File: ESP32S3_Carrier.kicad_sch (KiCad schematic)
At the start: 63 parts, among them J1 CC1101 433MHz SMA, J2 NRF24L01+PA+LNA #1, J3 NRF24L01+PA+LNA #2, J4 PN532 V3 (I2C), J5 OLED 1.3in SH1106 I2C, J6 Catalex microSD, J7 RDM6300 125kHz, J8 125kHz coil, J9 Si5351 clock gen (3x SMA), Q1 PN2222A, Q2 PN2222A, Q3 AO3401A, SW1 UP, SW2 DOWN, SW3 LEFT, SW4 RIGHT, SW5 OK, SW6 BACK, SW7 MODULE PWR, U1 ESP32-S3-DevKitC-1 N16R8, U2 AMS1117-3.3, U3 VS1838B

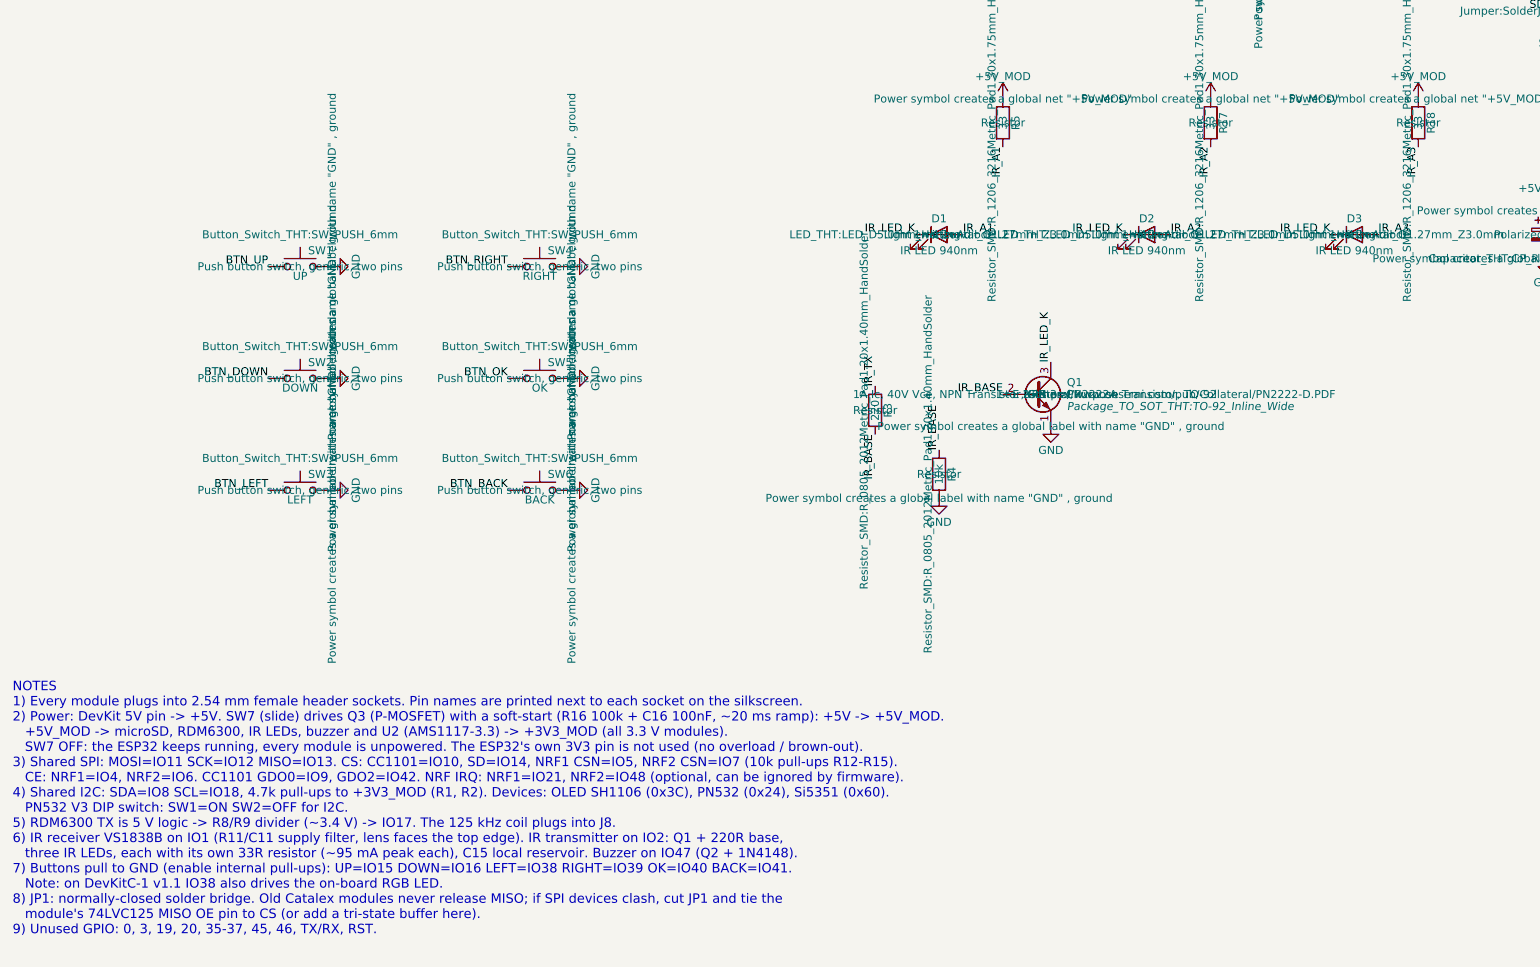
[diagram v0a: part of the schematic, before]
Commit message: IR LED resistors 33R -> 47R, README notes
- 47R per IR LED (~67 mA, ~0.21 W) so a stuck-high IO2 stays inside the 1206 rating
- README: drive IO2 only with the 38 kHz carrier; how to handle starved_thermal after a re-route

Co-Authored-By: Claude Opus 5.5 <noreply@anthropic.com>
Claude-Session: https://claude.ai/code/session_01M7B8FMVeVb1bqPRBZwSV29
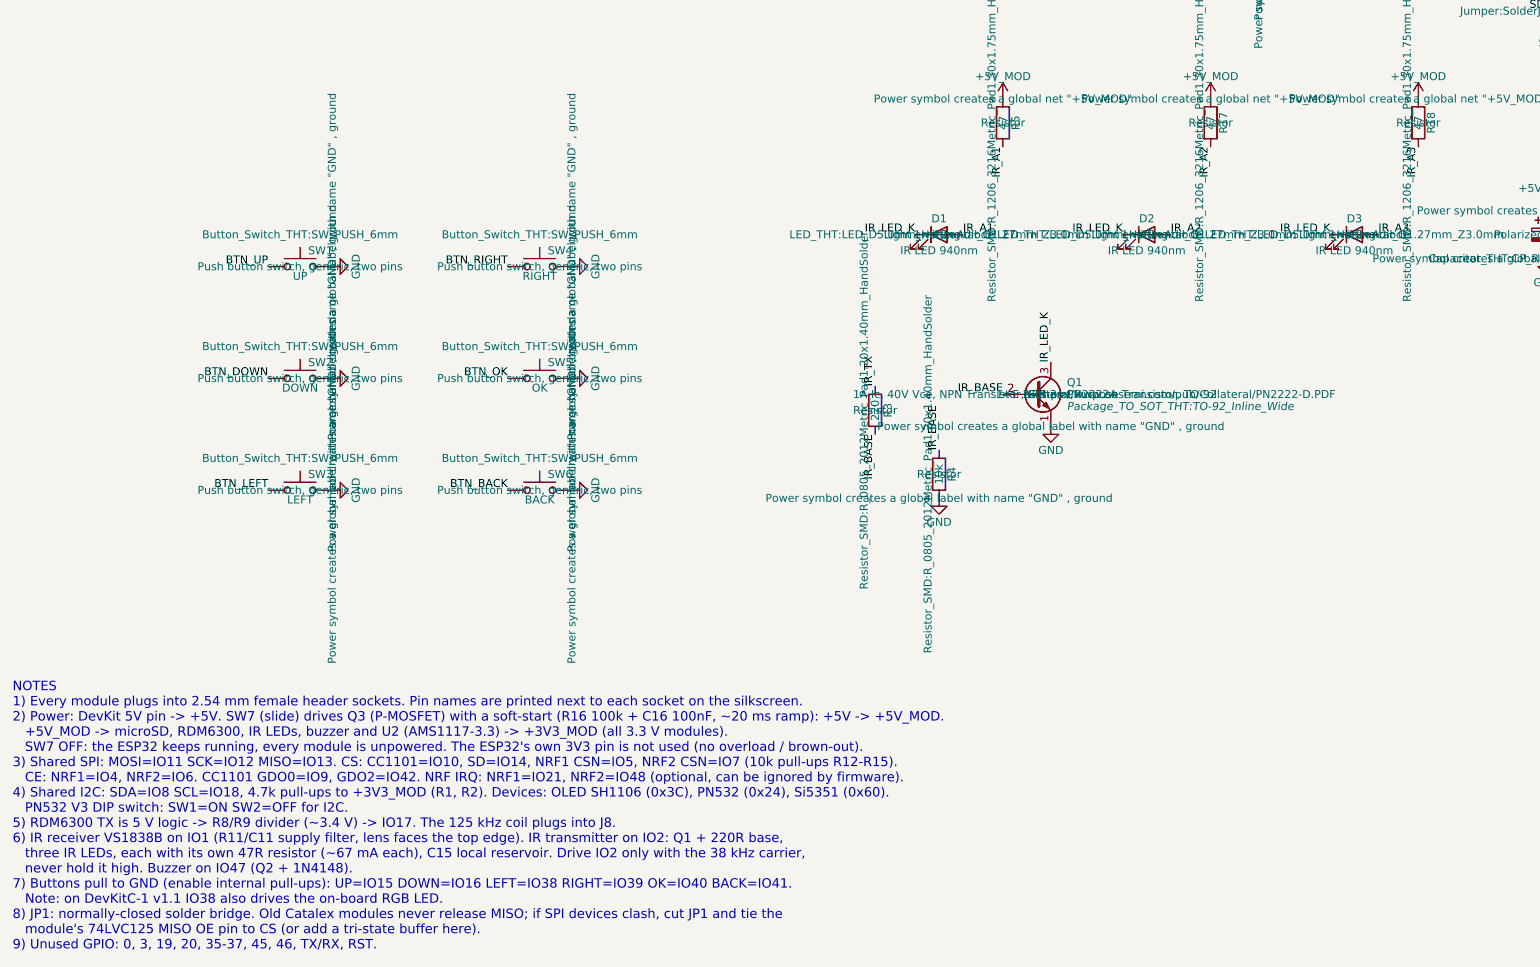
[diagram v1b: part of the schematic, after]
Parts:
- R17, R18, R5: value 33 -> 47
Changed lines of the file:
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@@
 			)
 		)
-		(property "Value" "33"
+		(property "Value" "47"
 			(at 177.8 231.14 90)
 			(effects
@@
 			)
 		)
-		(property "Value" "33"
+		(property "Value" "47"
 			(at 210.82 231.14 90)
 			(effects
@@
 			)
 		)
-		(property "Value" "33"
+		(property "Value" "47"
 			(at 243.84 231.14 90)
 			(effects
@@
 		)
 	)
-	(text "NOTES\n1) Every module plugs into 2.54 mm female header sockets. Pin names are printed next to each socket on the silkscreen.\n2) Power: DevKit 5V pin -> +5V. SW7 (slide) drives Q3 (P-MOSFET) with a soft-start (R16 100k + C16 100nF, ~20 ms ramp): +5V -> +5V_MOD.\n   +5V_MOD -> microSD, RDM6300, IR LEDs, buzzer and U2 (AMS1117-3.3) -> +3V3_MOD (all 3.3 V modules).\n   SW7 OFF: the ESP32 keeps running, every module is unpowered. The ESP32's own 3V3 pin is not used (no overload / brown-out).\n3) Shared SPI: MOSI=IO11 SCK=IO12 MISO=IO13. CS: CC1101=IO10, SD=IO14, NRF1 CSN=IO5, NRF2 CSN=IO7 (10k pull-ups R12-R15).\n   CE: NRF1=IO4, NRF2=IO6. CC1101 GDO0=IO9, GDO2=IO42. NRF IRQ: NRF1=IO21, NRF2=IO48 (optional, can be ignored by firmware).\n4) Shared I2C: SDA=IO8 SCL=IO18, 4.7k pull-ups to +3V3_MOD (R1, R2). Devices: OLED SH1106 (0x3C), PN532 (0x24), Si5351 (0x60).\n   PN532 V3 DIP switch: SW1=ON SW2=OFF for I2C.\n5) RDM6300 TX is 5 V logic -> R8/R9 divider (~3.4 V) -> IO17. The 125 kHz coil plugs into J8.\n6) IR receiver VS1838B on IO1 (R11/C11 supply filter, lens faces the top edge). IR transmitter on IO2: Q1 + 220R base,\n   three IR LEDs, each with its own 33R resistor (~95 mA peak each), C15 local reservoir. Buzzer on IO47 (Q2 + 1N4148).\n7) Buttons pull to GND (enable internal pull-ups): UP=IO15 DOWN=IO16 LEFT=IO38 RIGHT=IO39 OK=IO40 BACK=IO41.\n   Note: on DevKitC-1 v1.1 IO38 also drives the on-board RGB LED.\n8) JP1: normally-closed solder bridge. Old Catalex modules never release MISO; if SPI devices clash, cut JP1 and tie the\n   module's 74LVC125 MISO OE pin to CS (or add a tri-state buffer here).\n9) Unused GPIO: 0, 3, 19, 20, 35-37, 45, 46, TX/RX, RST."
+	(text "NOTES\n1) Every module plugs into 2.54 mm female header sockets. Pin names are printed next to each socket on the silkscreen.\n2) Power: DevKit 5V pin -> +5V. SW7 (slide) drives Q3 (P-MOSFET) with a soft-start (R16 100k + C16 100nF, ~20 ms ramp): +5V -> +5V_MOD.\n   +5V_MOD -> microSD, RDM6300, IR LEDs, buzzer and U2 (AMS1117-3.3) -> +3V3_MOD (all 3.3 V modules).\n   SW7 OFF: the ESP32 keeps running, every module is unpowered. The ESP32's own 3V3 pin is not used (no overload / brown-out).\n3) Shared SPI: MOSI=IO11 SCK=IO12 MISO=IO13. CS: CC1101=IO10, SD=IO14, NRF1 CSN=IO5, NRF2 CSN=IO7 (10k pull-ups R12-R15).\n   CE: NRF1=IO4, NRF2=IO6. CC1101 GDO0=IO9, GDO2=IO42. NRF IRQ: NRF1=IO21, NRF2=IO48 (optional, can be ignored by firmware).\n4) Shared I2C: SDA=IO8 SCL=IO18, 4.7k pull-ups to +3V3_MOD (R1, R2). Devices: OLED SH1106 (0x3C), PN532 (0x24), Si5351 (0x60).\n   PN532 V3 DIP switch: SW1=ON SW2=OFF for I2C.\n5) RDM6300 TX is 5 V logic -> R8/R9 divider (~3.4 V) -> IO17. The 125 kHz coil plugs into J8.\n6) IR receiver VS1838B on IO1 (R11/C11 supply filter, lens faces the top edge). IR transmitter on IO2: Q1 + 220R base,\n   three IR LEDs, each with its own 47R resistor (~67 mA each), C15 local reservoir. Drive IO2 only with the 38 kHz carrier,\n   never hold it high. Buzzer on IO47 (Q2 + 1N4148).\n7) Buttons pull to GND (enable internal pull-ups): UP=IO15 DOWN=IO16 LEFT=IO38 RIGHT=IO39 OK=IO40 BACK=IO41.\n   Note: on DevKitC-1 v1.1 IO38 also drives the on-board RGB LED.\n8) JP1: normally-closed solder bridge. Old Catalex modules never release MISO; if SPI devices clash, cut JP1 and tie the\n   module's 74LVC125 MISO OE pin to CS (or add a tri-state buffer here).\n9) Unused GPIO: 0, 3, 19, 20, 35-37, 45, 46, TX/RX, RST."
 		(exclude_from_sim no)
 		(at 20.32 320.04 0)

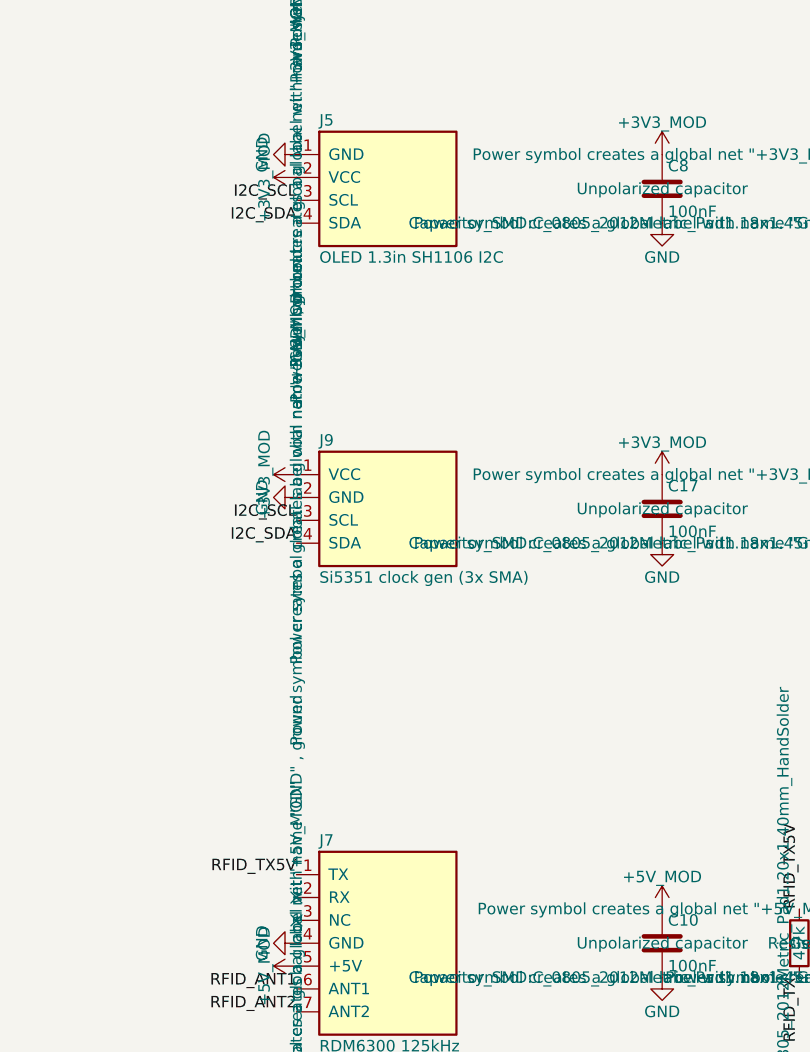
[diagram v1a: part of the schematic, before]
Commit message: Si5351: match the real 7-pin module (30.7x21.6 mm)
- 1x7 socket: 0, 1, 2, SCL, SDA, GND, VIN (VIN square pad), header 2.2 mm from the edge, centred
- Only SCL/SDA/GND/VIN connected; VIN on +3V3_MOD (module level shifter pulls I2C to VIN)
- CC1101 2x4 orientation confirmed by the owner
- Re-routed: ERC 0/0, DRC 0 (schematic parity), 277 stitching vias

Co-Authored-By: Claude Opus 5.5 <noreply@anthropic.com>
Claude-Session: https://claude.ai/code/session_01M7B8FMVeVb1bqPRBZwSV29
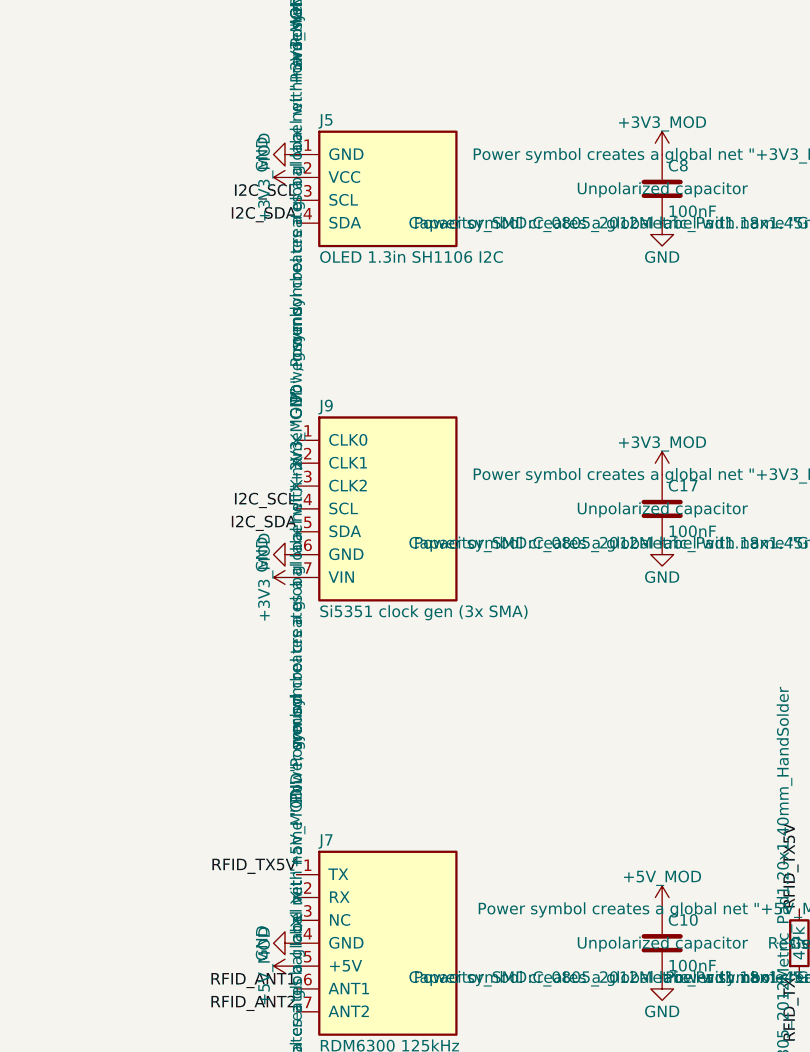
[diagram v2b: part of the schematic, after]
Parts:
- J9: symbol Carrier:Si5351_I2C -> Carrier:Si5351_7pin
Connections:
- net +3V3_MOD: now also J9.7 (VIN); no longer J9.1 (VCC)
- net GND: now also J9.6 (GND); no longer J9.2 (GND)
- net I2C_SCL: now also J9.4 (SCL); no longer J9.3 (SCL)
- net I2C_SDA: now also J9.5 (SDA); no longer J9.4 (SDA)
- no-connect marks 17 -> 20
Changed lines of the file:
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@@
 	)
 	(symbol
-		(lib_id "Carrier:Si5351_I2C")
+		(lib_id "Carrier:Si5351_7pin")
 		(at 360.68 134.62 0)
 		(unit 1)
@@
 		(dnp no)
 		(property "Reference" "J9"
-			(at 353.06 127 0)
+			(at 353.06 123.19 0)
 			(effects
 				(font
@@
 		)
 		(property "Value" "Si5351 clock gen (3x SMA)"
-			(at 353.06 142.24 0)
+			(at 353.06 146.05 0)
 			(effects
 				(font
@@
 			)
 		)
-		(property "Description" "Si5351 clock generator module, 3x SMA, 4-pin I2C"
+		(property "Description" "Si5351A clock generator module (CJMCU/Adafruit style), 3x SMA, 7-pin header 0,1,2,SCL,SDA,GND,VIN"
 			(at 360.68 134.62 0)
 			(effects
@@
 		)
 		(pin "4"
+		)
+		(pin "5"
+		)
+		(pin "6"
+		)
+		(pin "7"
 		)
 		(instances
@@
 		)
 	)
+	(no_connect
+		(at 350.52 127)
+	)
+	(no_connect
+		(at 350.52 129.54)
+	)
+	(no_connect
+		(at 350.52 132.08)
+	)
+	(label "I2C_SCL"
+		(at 350.52 134.62 180)
+		(effects
+			(font
+				(size 1.27 1.27)
+			)
+			(justify right bottom)
+		)
+	)
+	(label "I2C_SDA"
+		(at 350.52 137.16 180)
+		(effects
+			(font
+				(size 1.27 1.27)
+			)
+			(justify right bottom)
+		)
+	)
 	(symbol
-		(lib_id "Carrier:+3V3_MOD")
-		(at 350.52 130.81 90)
+		(lib_id "power:GND")
+		(at 350.52 139.7 270)
 		(unit 1)
 		(exclude_from_sim no)
@@
 		(dnp no)
 		(property "Reference" "#PWR020"
-			(at 354.33 130.81 0)
-			(effects
-				(font
-					(size 1.27 1.27)
-				)
-				(hide yes)
-			)
-		)
-		(property "Value" "+3V3_MOD"
-			(at 346.964 130.81 0)
+			(at 344.17 139.7 0)
+			(effects
+				(font
+					(size 1.27 1.27)
+				)
+				(hide yes)
+			)
+		)
+		(property "Value" "GND"
+			(at 346.71 139.7 0)
 			(effects
 				(font
@@
 		)
 		(property "Footprint" ""
-			(at 350.52 130.81 0)
+			(at 350.52 139.7 0)
 			(effects
 				(font
@@
 		)
 		(property "Datasheet" ""
-			(at 350.52 130.81 0)
-			(effects
-				(font
-					(size 1.27 1.27)
-				)
-			)
-		)
-		(property "Description" "Power symbol creates a global net \"+3V3_MOD\""
-			(at 350.52 130.81 0)
+			(at 350.52 139.7 0)
+			(effects
+				(font
+					(size 1.27 1.27)
+				)
+			)
+		)
+		(property "Description" "Power symbol creates a global label with name \"GND\" , ground"
+			(at 350.52 139.7 0)
 			(effects
 				(font
@@
 	)
 	(symbol
-		(lib_id "power:GND")
-		(at 350.52 133.35 270)
+		(lib_id "Carrier:+3V3_MOD")
+		(at 350.52 142.24 90)
 		(unit 1)
 		(exclude_from_sim no)
@@
 		(dnp no)
 		(property "Reference" "#PWR021"
-			(at 344.17 133.35 0)
-			(effects
-				(font
-					(size 1.27 1.27)
-				)
-				(hide yes)
-			)
-		)
-		(property "Value" "GND"
-			(at 346.71 133.35 0)
+			(at 354.33 142.24 0)
+			(effects
+				(font
+					(size 1.27 1.27)
+				)
+				(hide yes)
+			)
+		)
+		(property "Value" "+3V3_MOD"
+			(at 346.964 142.24 0)
 			(effects
 				(font
@@
 		)
 		(property "Footprint" ""
-			(at 350.52 133.35 0)
+			(at 350.52 142.24 0)
 			(effects
 				(font
@@
 		)
 		(property "Datasheet" ""
-			(at 350.52 133.35 0)
-			(effects
-				(font
-					(size 1.27 1.27)
-				)
-			)
-		)
-		(property "Description" "Power symbol creates a global label with name \"GND\" , ground"
-			(at 350.52 133.35 0)
+			(at 350.52 142.24 0)
+			(effects
+				(font
+					(size 1.27 1.27)
+				)
+			)
+		)
+		(property "Description" "Power symbol creates a global net \"+3V3_MOD\""
+			(at 350.52 142.24 0)
 			(effects
 				(font
@@
 		)
 	)
-	(label "I2C_SCL"
-		(at 350.52 135.89 180)
-		(effects
-			(font
-				(size 1.27 1.27)
-			)
-			(justify right bottom)
-		)
-	)
-	(label "I2C_SDA"
-		(at 350.52 138.43 180)
-		(effects
-			(font
-				(size 1.27 1.27)
-			)
-			(justify right bottom)
-		)
-	)

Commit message: Rev 1.2: 18650 battery power (TP4056 + MT3608 + main switch)
- JST-PH 18650 connector, protected TP4056 charger at the left edge
- Main power switch (SW8 + AO3401A), MT3608 boost to 5.3 V, SS34 diode-OR with DevKit USB
- Battery voltage divider on IO3
- Board 116x200 mm; ERC 0/0, DRC 0 (schematic parity), 100% routed

Co-Authored-By: Claude Opus 5.5 <noreply@anthropic.com>
Claude-Session: https://claude.ai/code/session_01M7B8FMVeVb1bqPRBZwSV29
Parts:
- added C18: 100nF, Capacitor_SMD:C_0805_2012Metric_Pad1.18x1.45mm_HandSolder, symbol Device:C
- added D5: SS34, Diode_SMD:D_SMA_Handsoldering, symbol Device:D_Schottky
- added J10: 18650 BAT, Connector_JST:JST_PH_B2B-PH-K_1x02_P2.00mm_Vertical, symbol Connector_Generic:Conn_01x02
- added Q4: AO3401A, Package_TO_SOT_SMD:SOT-23, symbol Carrier:AO3401A
- added R19, R20, R21: 100k, Resistor_SMD:R_0805_2012Metric_Pad1.20x1.40mm_HandSolder, symbol Device:R
- added SW8: MAIN PWR, Button_Switch_THT:SW_Slide_SPDT_Angled_CK_OS102011MA1Q, symbol Switch:SW_SPDT
- added U4: TP4056 module (protected), Carrier:TP4056_Module_Pads, symbol Carrier:TP4056_Module
- added U5: MT3608 boost module (set 5.3V), Carrier:MT3608_Module_Pads, symbol Carrier:MT3608_Module
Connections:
- net +5V: now also D5.1 (K)
- net GND: now also C18.2, R21.2, SW8.1 (A), U4.4 (OUT-), U5.2 (VIN-), U5.4 (VOUT-)
- net BAT_SENSE: now reaches U1.13 (IO3)
- net BAT_SENSE: now also C18.1, R20.2, R21.1
- new net BAT_GATE: Q4.1 (G), R19.2, SW8.2 (B)
- new net BAT_N: J10.2 (Pin_2), U4.3 (B-)
- new net BOOST_5V: D5.2 (A), U5.3 (VOUT+)
- new net VBAT: J10.1 (Pin_1), Q4.2 (S), R19.1, U4.1 (OUT+), U4.2 (B+)
- new net VBAT_SW: Q4.3 (D), R20.1, U5.1 (VIN+)
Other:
- note added: "ESP32-S3 CARRIER BOARD - rev 1.2 - 2026-10-22"
- note removed: "ESP32-S3 CARRIER BOARD - rev 1.1 - 2026-10-22"
